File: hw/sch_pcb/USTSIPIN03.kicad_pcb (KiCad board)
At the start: 2 copper layers, 70.6 x 50.3 mm, 102 parts, among them J1 HEADER_2x15, M1 HOLE, M2 HOLE, M3 HOLE, M4 HOLE, M5 RFShield_TwoPieces, Q1 2SK2394-6, U1 ISL21080CIH341Z-TK, U10 ISL21080DIH309, U11 AT24CS64-SSHM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

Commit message: Update silkscreen and title blocks.
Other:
- board text added: "USTSIPIN03A"
- board text removed: "AIRDOS04A sensor board"
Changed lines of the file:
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@@
     (effects (font (size 1.5 1.5) (thickness 0.2)))
   )
-  (gr_text "AIRDOS04A sensor board" (at 149.1488 127.7874) (layer "B.Cu")
+  (gr_text "USTSIPIN03A" (at 149.1488 127.7874) (layer "B.Cu")
     (effects (font (size 1.5 1.5) (thickness 0.3)) (justify mirror))
   )
@@
     (effects (font (size 0.8 0.8) (thickness 0.15) bold) (justify left bottom))
   )
-  (gr_text "AIRDOS04A sensor board" (at 128.524 106.5276 90) (layer "F.SilkS")
+  (gr_text "USTSIPIN03A" (at 128.8034 101.1428 90) (layer "F.SilkS")
     (effects (font (size 1.5 1.5) (thickness 0.3)))
   )

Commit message: Update PCB from schematics.
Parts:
- C16: value 1nF NP0 -> 1nF
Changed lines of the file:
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@@
   (paper "A4")
   (title_block
-    (title "AIRDOS04")
-    (date "%d. %m. %Y")
+    (title "USTSIPIN03A")
+    (date "2023-11-20")
     (rev "REV")
     (company "Universal Scientific Technologies s.r.o.")
@@
     (descr "Mounting hole, Befestigungsbohrung, 3mm, No Annular, Kein Restring,")
     (tags "Mounting hole, Befestigungsbohrung, 3mm, No Annular, Kein Restring,")
-    (property "Sheetfile" "AIRDOS04_sensor.kicad_sch")
+    (property "Sheetfile" "USTSIPIN03.kicad_sch")
     (property "Sheetname" "")
     (property "ki_keywords" "HOLE, X, M")
@@
     (descr "Mounting hole, Befestigungsbohrung, 3mm, No Annular, Kein Restring,")
     (tags "Mounting hole, Befestigungsbohrung, 3mm, No Annular, Kein Restring,")
-    (property "Sheetfile" "AIRDOS04_sensor.kicad_sch")
+    (property "Sheetfile" "USTSIPIN03.kicad_sch")
     (property "Sheetname" "")
     (property "ki_keywords" "HOLE, X, M")
@@
     (descr "Mounting hole, Befestigungsbohrung, 3mm, No Annular, Kein Restring,")
     (tags "Mounting hole, Befestigungsbohrung, 3mm, No Annular, Kein Restring,")
-    (property "Sheetfile" "AIRDOS04_sensor.kicad_sch")
+    (property "Sheetfile" "USTSIPIN03.kicad_sch")
     (property "Sheetname" "")
     (property "ki_keywords" "HOLE, X, M")
@@
     (descr "Mounting hole, Befestigungsbohrung, 3mm, No Annular, Kein Restring,")
     (tags "Mounting hole, Befestigungsbohrung, 3mm, No Annular, Kein Restring,")
-    (property "Sheetfile" "AIRDOS04_sensor.kicad_sch")
+    (property "Sheetfile" "USTSIPIN03.kicad_sch")
     (property "Sheetname" "")
     (property "ki_keywords" "HOLE, X, M")
@@
     (property "Sheetfile" "analogue_backend.kicad_sch")
     (property "Sheetname" "analogue_backend")
-    (property "UST_ID" "5c70984812875079b91f8bf2")
+    (property "UST_ID" "5c70984712875079b91f8b4c")
     (property "ki_description" "Unpolarized capacitor")
     (property "ki_keywords" "cap capacitor")
@@
     (property "Sheetfile" "analogue_backend.kicad_sch")
     (property "Sheetname" "analogue_backend")
-    (property "UST_ID" "5d47bf10128750448e6b4652")
+    (property "UST_ID" "5c70984812875079b91f8ba6")
     (property "ki_description" "Unpolarized capacitor")
     (property "ki_keywords" "cap capacitor")
@@
         (effects (font (size 1 1) (thickness 0.15)) (justify mirror))
     )
-    (fp_text value "1nF NP0" (at 0 -1.68 90) (layer "B.Fab") hide
+    (fp_text value "1nF" (at 0 -1.68 90) (layer "B.Fab") hide
         (effects (font (size 1 1) (thickness 0.15)) (justify mirror))
     )
@@
     (property "Sheetfile" "analogue_backend.kicad_sch")
     (property "Sheetname" "analogue_backend")
-    (property "UST_ID" "")
+    (property "UST_ID" "5c70984612875079b91f899f")
     (property "ki_description" "Resistor")
     (property "ki_keywords" "R res resistor")
@@
     (property "Sheetfile" "analogue_backend.kicad_sch")
     (property "Sheetname" "analogue_backend")
-    (property "UST_ID" "5c70984812875079b91f8bf2")
+    (property "UST_ID" "5c70984712875079b91f8b4c")
     (property "ki_description" "Unpolarized capacitor")
     (property "ki_keywords" "cap capacitor")
@@
     (property "Sheetfile" "analogue_backend.kicad_sch")
     (property "Sheetname" "analogue_backend")
-    (property "UST_ID" "6508260b462c6d9e720541f1")
+    (property "UST_ID" "5c70984712875079b91f8b4c")
     (property "ki_description" "Unpolarized capacitor")
     (property "ki_keywords" "cap capacitor")
@@
     (property "Sheetfile" "analogue_backend.kicad_sch")
     (property "Sheetname" "analogue_backend")
-    (property "UST_ID" "")
+    (property "UST_ID" "65555d4795a79cc5ac409b41")
     (property "ki_description" "74AUC1G74, Single D Flip-Flop, Low-Voltage CMOS")
     (property "ki_keywords" "Single D Flip-Flop D CMOS")
@@
     (property "Sheetfile" "interface.kicad_sch")
     (property "Sheetname" "interface")
+    (property "UST_ID" "65555a850c8d609e3e79abde")
     (property "ki_description" "Dual supply translating transceiver, 3-state, 2-bit, VSSOP-8")
     (property "ki_keywords" "Level-Shifter CMOS-TTL-Translation")
@@
     (property "Sheetfile" "analogue_backend.kicad_sch")
     (property "Sheetname" "analogue_backend")
+    (property "UST_ID" "651eaece462c6d9e72055763")
     (property "ki_description" "Dual channel 16-bit SAR Analog to Digital Converter, 5V supply, 150ksps, SPI interface")
     (property "ki_keywords" "adc 2ch")
@@
     (property "Sheetfile" "analogue_backend.kicad_sch")
     (property "Sheetname" "analogue_backend")
-    (property "UST_ID" "5d47bf10128750448e6b4652")
+    (property "UST_ID" "5c70984812875079b91f8ba6")
     (property "ki_description" "Unpolarized capacitor")
     (property "ki_keywords" "cap capacitor")
@@
     (property "Sheetfile" "analogue_backend.kicad_sch")
     (property "Sheetname" "analogue_backend")
-    (property "UST_ID" "")
+    (property "UST_ID" "6555591d0c8d609e3e79abc1")
     (property "ki_description" "2.0V 25μA Micropower Voltage Reference, SOT-23")
     (property "ki_keywords" "Micropower Voltage Reference 2.0V")
@@
     (property "Sheetfile" "PIN_detector.kicad_sch")
     (property "Sheetname" "PIN_detector")
-    (property "UST_ID" "")
+    (property "UST_ID" "5c70984612875079b91f899f")
     (property "ki_description" "Resistor")
     (property "ki_keywords" "R res resistor")
@@
     (property "Sheetfile" "PIN_detector.kicad_sch")
     (property "Sheetname" "PIN_detector")
-    (property "UST_ID" "5c70984812875079b91f8bf2")
+    (property "UST_ID" "5c70984712875079b91f8b4c")
     (property "ki_description" "Unpolarized capacitor, small symbol")
     (property "ki_keywords" "capacitor cap")
@@
     (descr "Circular Fiducial, 1mm bare copper, 2mm soldermask opening (Level A)")
     (tags "fiducial")
-    (property "Sheetfile" "AIRDOS04_sensor.kicad_sch")
+    (property "Sheetfile" "USTSIPIN03.kicad_sch")
     (property "Sheetname" "")
+    (property "UST_ID" "")
+    (property "exclude_from_bom" "")
     (property "ki_description" "Fiducial Marker")
     (property "ki_keywords" "fiducial marker")
-    (attr smd)
+    (attr smd exclude_from_bom)
     (fp_text reference "FID4" (at 0 2 -270) (layer "B.SilkS") hide
         (effects (font (size 1 1) (thickness 0.15)) (justify mirror))
@@
     (property "Sheetfile" "PIN_detector.kicad_sch")
     (property "Sheetname" "PIN_detector")
-    (property "UST_ID" "5c70984812875079b91f8bf2")
+    (property "UST_ID" "5c70984712875079b91f8b4c")
     (property "ki_description" "Unpolarized capacitor")
     (property "ki_keywords" "cap capacitor")
@@
     (descr "Circular Fiducial, 1mm bare copper, 2mm soldermask opening (Level A)")
     (tags "fiducial")
-    (property "Sheetfile" "AIRDOS04_sensor.kicad_sch")
+    (property "Sheetfile" "USTSIPIN03.kicad_sch")
     (property "Sheetname" "")
+    (property "UST_ID" "")
+    (property "exclude_from_bom" "")
     (property "ki_description" "Fiducial Marker")
     (property "ki_keywords" "fiducial marker")
-    (attr smd)
+    (attr smd exclude_from_bom)
     (fp_text reference "FID2" (at -0.254 2.159) (layer "B.SilkS") hide
         (effects (font (size 1 1) (thickness 0.15)) (justify mirror))
@@
     (property "Sheetfile" "analogue_backend.kicad_sch")
     (property "Sheetname" "analogue_backend")
-    (property "UST_ID" "")
+    (property "UST_ID" "5c70984612875079b91f899f")
     (property "ki_description" "Resistor")
     (property "ki_keywords" "R res resistor")
@@
     (descr "Circular Fiducial, 1mm bare copper, 2mm soldermask opening (Level A)")
     (tags "fiducial")
-    (property "Sheetfile" "AIRDOS04_sensor.kicad_sch")
+    (property "Sheetfile" "USTSIPIN03.kicad_sch")
     (property "Sheetname" "")
+    (property "UST_ID" "")
+    (property "exclude_from_bom" "")
     (property "ki_description" "Fiducial Marker")
     (property "ki_keywords" "fiducial marker")
-    (attr smd)
+    (attr smd exclude_from_bom)
     (fp_text reference "FID1" (at 0.508 -2.479) (layer "B.SilkS") hide
         (effects (font (size 1 1) (thickness 0.15)) (justify mirror))
@@
     (property "Sheetfile" "interface.kicad_sch")
     (property "Sheetname" "interface")
+    (property "UST_ID" "65555a850c8d609e3e79abde")
     (property "ki_description" "Dual supply translating transceiver, 3-state, 2-bit, VSSOP-8")
     (property "ki_keywords" "Level-Shifter CMOS-TTL-Translation")
@@
     (property "Sheetfile" "interface.kicad_sch")
     (property "Sheetname" "interface")
-    (property "UST_ID" "")
+    (property "UST_ID" "5c70984612875079b91f899f")
     (property "ki_description" "Resistor")
     (property "ki_keywords" "R res resistor")
@@
     (descr "Circular Fiducial, 1mm bare copper, 2mm soldermask opening (Level A)")
     (tags "fiducial")
-    (property "Sheetfile" "AIRDOS04_sensor.kicad_sch")
+    (property "Sheetfile" "USTSIPIN03.kicad_sch")
     (property "Sheetname" "")
+    (property "UST_ID" "")
+    (property "exclude_from_bom" "")
     (property "ki_description" "Fiducial Marker")
     (property "ki_keywords" "fiducial marker")
-    (attr smd)
+    (attr smd exclude_from_bom)
     (fp_text reference "FID3" (at 0 2 -270) (layer "B.SilkS") hide
         (effects (font (size 1 1) (thickness 0.15)) (justify mirror))
@@
     (property "Sheetfile" "interface.kicad_sch")
     (property "Sheetname" "interface")
-    (property "UST_ID" "")
+    (property "UST_ID" "5c70984612875079b91f899f")
     (property "ki_description" "Resistor")
     (property "ki_keywords" "R res resistor")
@@
     (property "Sheetfile" "interface.kicad_sch")
     (property "Sheetname" "interface")
+    (property "UST_ID" "65555a850c8d609e3e79abde")
     (property "ki_description" "Dual supply translating transceiver, 3-state, 2-bit, VSSOP-8")
     (property "ki_keywords" "Level-Shifter CMOS-TTL-Translation")

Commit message: Edit logo reference value.
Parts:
- renumbered G*** to G1
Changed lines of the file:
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@@
     (at 121.285 100.457 90)
     (attr through_hole board_only)
-    (fp_text reference "G***" (at 0 0 90) (layer "F.SilkS") hide
+    (fp_text reference "G1" (at 0 0 90) (layer "F.SilkS") hide
         (effects (font (size 1.524 1.524) (thickness 0.3)))
     )

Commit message: Flip side of pinheader connector. Resolve #7
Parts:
- J1: moved to B.Cu
- turned J1 to -90 degrees
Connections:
- J1 pad 10: /interface/A0 -> unconnected-(J1-Pad10)
- J1 pad 11: /interface/RX -> /interface/A1
- J1 pad 12: /interface/A1 -> /interface/RX
- J1 pad 13: /interface/TX -> /interface/B1
- J1 pad 14: /interface/B1 -> /interface/TX
- J1 pad 15: /interface/SOCKET_MOSI -> /interface/B0
- J1 pad 16: /interface/B0 -> /interface/SOCKET_MOSI
- J1 pad 17: /interface/SOCKET_MISO -> /interface/C1
- J1 pad 18: /interface/C1 -> /interface/SOCKET_MISO
- J1 pad 19: /interface/SOCKET_SCLK -> /interface/C0
- J1 pad 20: /interface/C0 -> /interface/SOCKET_SCLK
- J1 pad 9: unconnected-(J1-Pad9) -> /interface/A0

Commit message: Swap power pins of input OpAMP. Reslove #6
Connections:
- U8 pad 2: Net-(U8-V+) -> GNDA
- U8 pad 5: GNDA -> Net-(U8-V+)
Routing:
- net GNDA: track 129.1 -> 127.4 mm, vias 11 -> 12

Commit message: Swap MISO and MOSI traces. Resolve #4
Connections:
- U12 pad 2: /interface/SOCKET_MISO -> /interface/SOCKET_MOSI
- U12 pad 7: /analogue_backend/SDO -> /analogue_backend/SDI
- U14 pad 3: /interface/SOCKET_MOSI -> /interface/SOCKET_MISO
- U14 pad 6: /analogue_backend/SDI -> /analogue_backend/SDO
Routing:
- net /interface/SOCKET_MISO: track 51.4 -> 60.2 mm
- net /interface/SOCKET_MOSI: track 55.7 -> 49.6 mm
- net /analogue_backend/SDI: track 10.1 -> 13.5 mm
- net /analogue_backend/SDO: track 13.5 -> 10.2 mm, vias 0 -> 2
- net /interface/B0: track 59.5 -> 62.4 mm
- net /analogue_backend/Set: track 55.9 -> 56.7 mm
- net GND: vias 17 -> 19
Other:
- board text added: "USTSIPIN03B"
- board text removed: "USTSIPIN03A"

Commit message: Attempt to improve #2.
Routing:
- net /analogue_backend/Set: track 56.7 -> 55.5 mm
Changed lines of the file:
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@@
     )
   )
+  (gr_rect (start 141.9098 101.720501) (end 170.618299 118.0846)
+    (stroke (width 0.15) (type solid)) (fill solid) (layer "F.Mask"))
   (gr_rect (start 113.194 79.854) (end 183.806 130.145999)
     (stroke (width 0.15) (type default)) (fill none) (layer "Edge.Cuts"))
@@
   (segment (start 139.3795 108.175) (end 139.1528 108.4017) (width 0.45) (layer "B.Cu") (net 46))
   (segment (start 141.9524 103.2898) (end 141.9524 102.134799) (width 0.45) (layer "B.Cu") (net 46))
-  (segment (start 116.1034 115.8748) (end 115.1382 114.9096) (width 0.45) (layer "F.Cu") (net 47))
-  (segment (start 118.745 89.7382) (end 118.795798 89.7382) (width 0.45) (layer "F.Cu") (net 47))
-  (segment (start 115.1382 93.345) (end 118.745 89.7382) (width 0.45) (layer "F.Cu") (net 47))
-  (segment (start 115.1382 114.9096) (end 115.1382 93.345) (width 0.45) (layer "F.Cu") (net 47))
-  (via (at 116.1034 115.8748) (size 0.8) (drill 0.4) (layers "F.Cu" "B.Cu") (net 47))
+  (segment (start 116.6114 116.459) (end 116.5606 116.5098) (width 0.45) (layer "F.Cu") (net 47))
+  (segment (start 116.6114 91.922598) (end 116.6114 116.459) (width 0.45) (layer "F.Cu") (net 47))
+  (segment (start 118.795798 89.7382) (end 116.6114 91.922598) (width 0.45) (layer "F.Cu") (net 47))
+  (via (at 116.5606 116.5098) (size 0.8) (drill 0.4) (layers "F.Cu" "B.Cu") (net 47))
   (via (at 118.795798 89.7382) (size 0.8) (drill 0.4) (layers "F.Cu" "B.Cu") (net 47))
   (segment (start 141.5034 89.7382) (end 118.795798 89.7382) (width 0.45) (layer "B.Cu") (net 47))
   (segment (start 141.5034 89.7382) (end 141.730457 89.7382) (width 0.3) (layer "B.Cu") (net 47))
-  (segment (start 116.1034 116.792) (end 116.1034 115.8748) (width 0.3) (layer "B.Cu") (net 47))
+  (segment (start 117.498 118.1866) (end 116.5606 117.2492) (width 0.3) (layer "B.Cu") (net 47))
+  (segment (start 118.248 118.1866) (end 117.498 118.1866) (width 0.3) (layer "B.Cu") (net 47))
   (segment (start 141.730457 89.7382) (end 142.365057 89.1036) (width 0.3) (layer "B.Cu") (net 47))
   (segment (start 142.365057 89.1036) (end 143.4956 89.1036) (width 0.3) (layer "B.Cu") (net 47))
-  (segment (start 117.498 118.1866) (end 116.1034 116.792) (width 0.3) (layer "B.Cu") (net 47))
-  (segment (start 118.248 118.1866) (end 117.498 118.1866) (width 0.3) (layer "B.Cu") (net 47))
+  (segment (start 116.5606 117.2492) (end 116.5606 116.5098) (width 0.3) (layer "B.Cu") (net 47))
   (segment (start 117.047229 118.6866) (end 118.248 118.6866) (width 0.3) (layer "B.Cu") (net 48))
   (segment (start 114.808 94.963437) (end 114.808 116.447371) (width 0.45) (layer "B.Cu") (net 48))

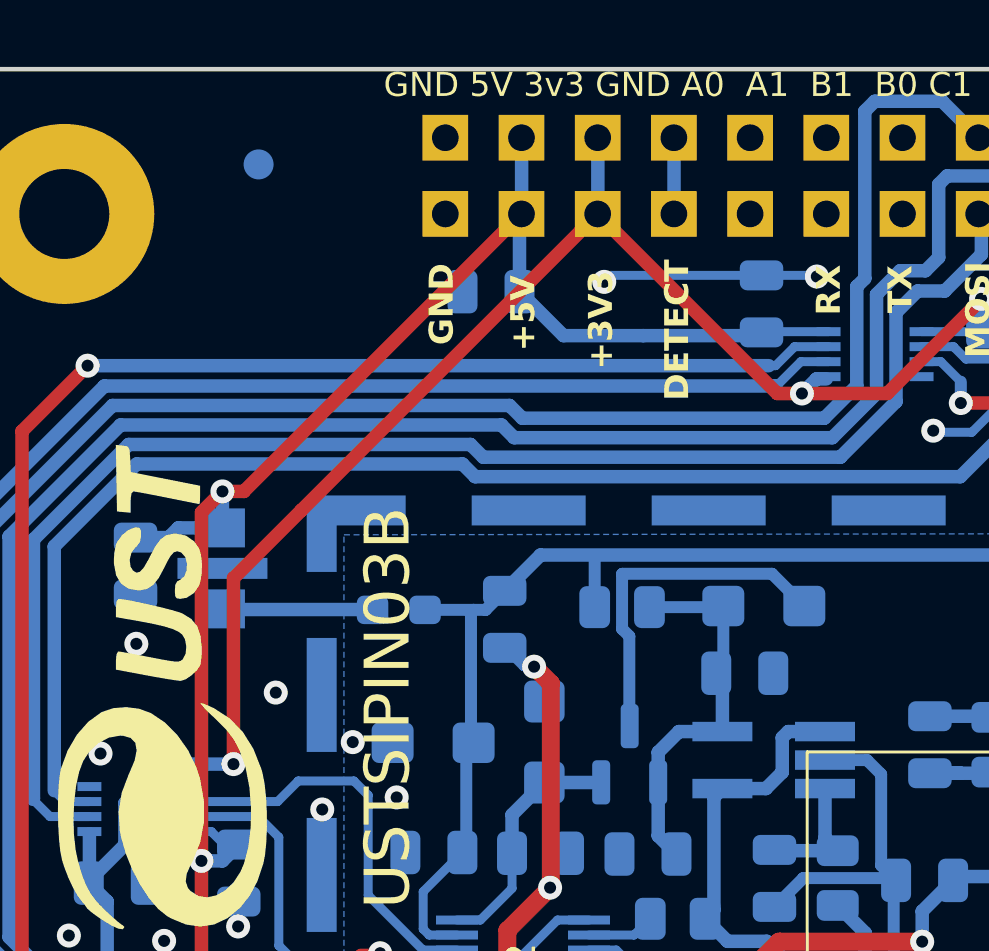
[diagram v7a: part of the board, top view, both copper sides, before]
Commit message: Add LDO to power 3.3V translators. Resolve #3
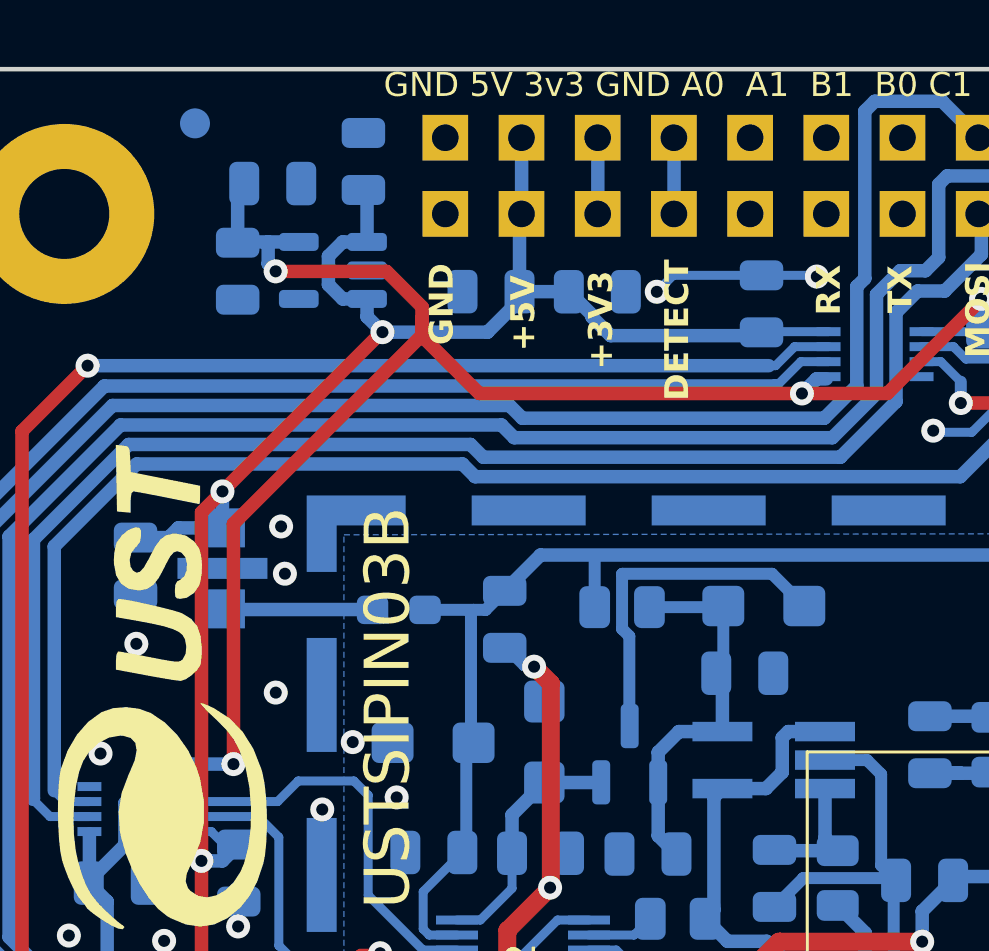
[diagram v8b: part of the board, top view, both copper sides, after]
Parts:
- added C49: 10uF, Capacitor_SMD:C_0805_2012Metric, B.Cu at (128.0, 82.9)
- added C50: 100nF, Capacitor_SMD:C_0805_2012Metric, B.Cu at (135.8, 87.3)
- added C51: 10uF, Capacitor_SMD:C_0805_2012Metric, B.Cu at (123.8, 86.6)
- added C52: 100nF, Capacitor_SMD:C_0805_2012Metric, B.Cu at (125.0, 83.7)
- added U15: MIC5504-3.3YM5-TR, Package_TO_SOT_SMD:SOT-23-5, B.Cu at (127.0, 86.6)
- moved FID3 2.52 mm to (122.4, 81.7)
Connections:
- C42 pad 1: /interface/3v3 -> +3.3V
- C44 pad 1: /interface/3v3 -> +3.3V
- C46 pad 1: /interface/3v3 -> +3.3V
- U12 pad 1: /interface/3v3 -> +3.3V
- U12 pad 5: /interface/3v3 -> +3.3V
- U13 pad 1: /interface/3v3 -> +3.3V
- U13 pad 5: /interface/3v3 -> +3.3V
- U14 pad 1: /interface/3v3 -> +3.3V
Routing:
- net +3.3V: track 0.00 -> 70.9 mm, vias 0 -> 4
- net /interface/3v3: track 63.4 -> 2.54 mm, vias 3 -> 0
- net +5VD: track 71.8 -> 77.9 mm, vias 5 -> 6
- net GND: track 22.0 -> 20.4 mm, vias 19 -> 21
